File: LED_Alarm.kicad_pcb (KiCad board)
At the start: 2 copper layers, 48.3 x 82.8 mm, 83 parts, among them Q301 Q_NPN_BCE, Q401 FDMA410NZT, Q402 FDMA410NZT, Q403 FDMA410NZT, Q501 FDMA410NZT, Q502 FDMA410NZT, Q503 FDMA410NZT, Q601 FDMA410NZT, Q602 FDMA410NZT, Q603 FDMA410NZT, Q701 FDMA410NZT, Q702 FDMA410NZT, Q703 FDMA410NZT, Q801 FDMA410NZT, Q802 FDMA410NZT, Q803 FDMA410NZT, U101 H11AA11, U102 ESP-12, U103 PCA9685PW, U201 MOC3020M, U202 TRIAC, U901 XC9263

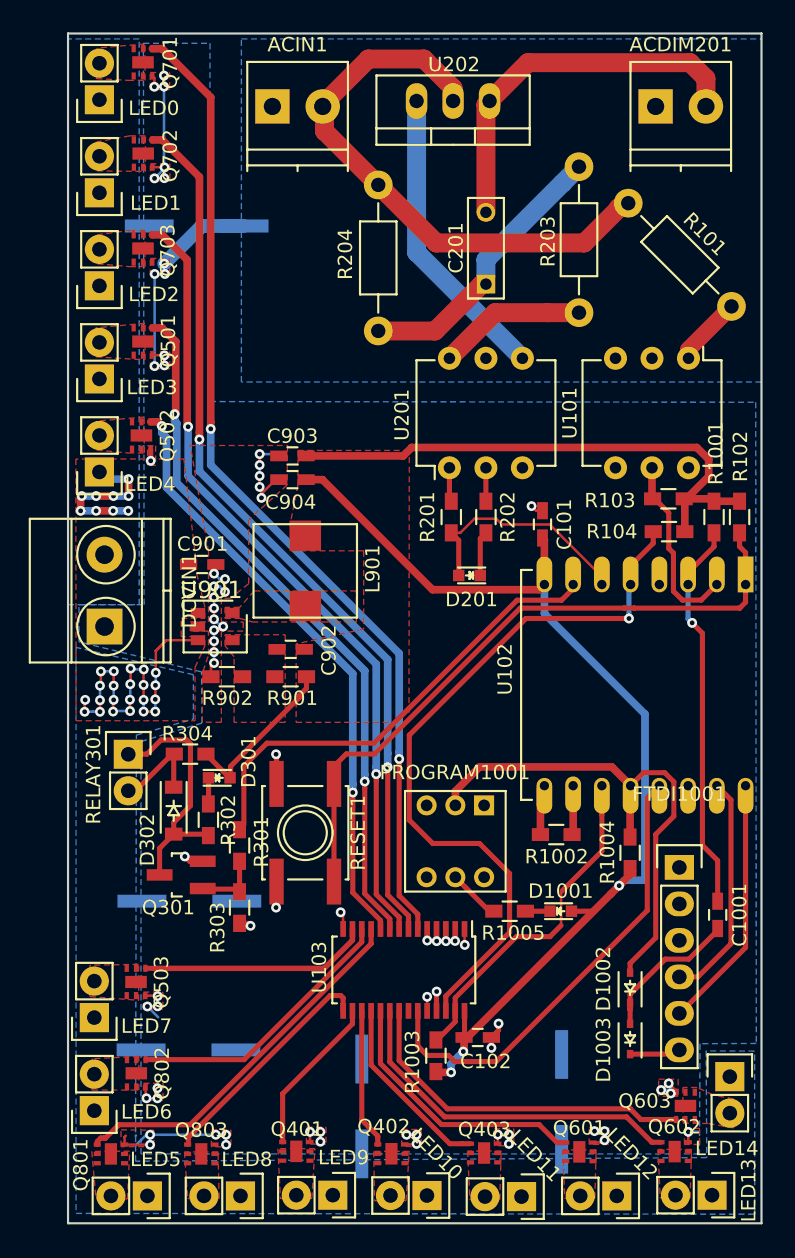
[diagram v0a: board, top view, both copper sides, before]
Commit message: After changes suggested in https://www.reddit.com/r/PrintedCircuitBoard/comments/54ctxv/pcb_review_of_a_pwm_esp8266_led_driver_board/
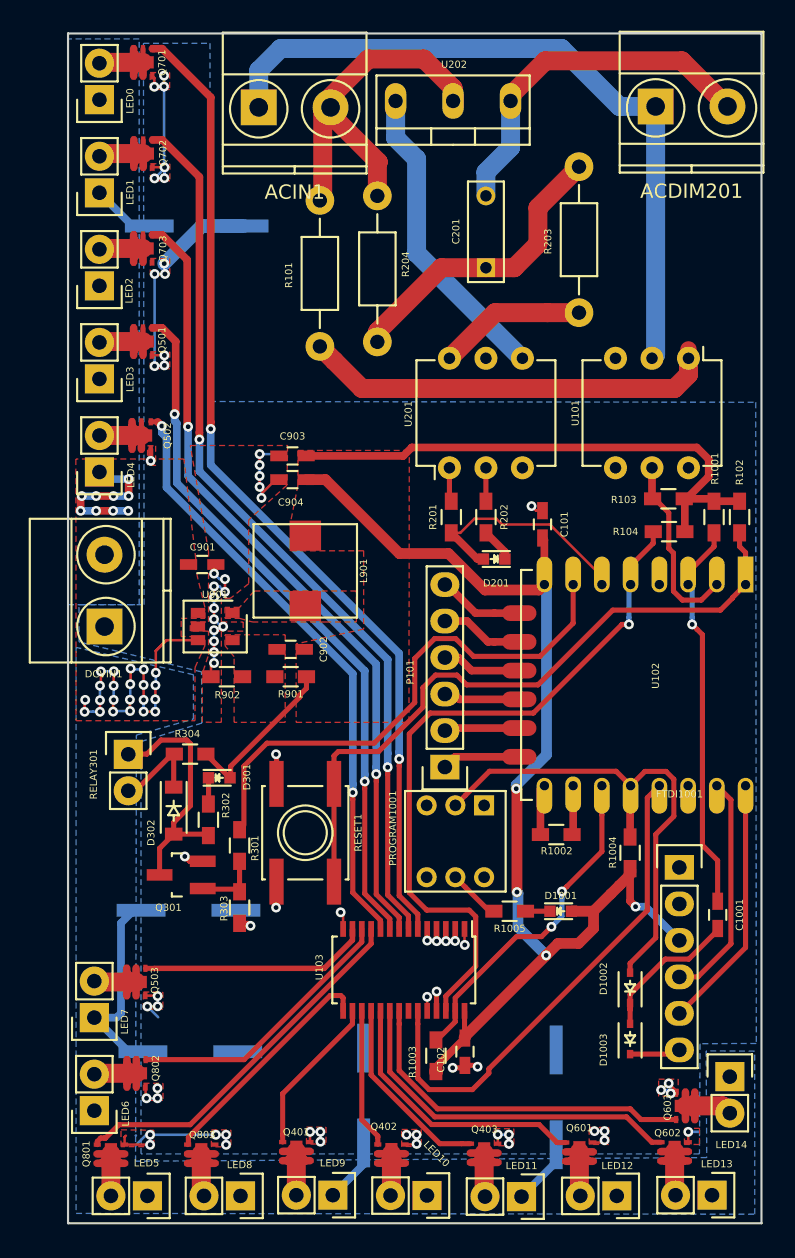
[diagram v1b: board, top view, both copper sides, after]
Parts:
- added P101: CONN_01X06, Pin_Headers:Pin_Header_Straight_1x06, F.Cu at (78.3, 88.8)
- ACDIM201, ACIN1: footprint Terminal_Blocks:TerminalBlock_Pheonix_PT-3.5mm_2pol -> Terminal_Blocks:TerminalBlock_Pheonix_MKDS1.5-2pol
- U102: footprint ESP8266:ESP-12 -> ESP8266:ESP-12E
- moved R101 21.5 mm to (69.6, 49.3), turned to 270 degrees
- moved D201 2.06 mm to (81.7, 74.3)
- moved C102 1.33 mm to (79.7, 108.6), turned to 270 degrees
- moved C201 1.14 mm to (81.2, 54.0)
- moved ACIN1 0.95 mm to (65.3, 42.9)
- moved C601 0.77 mm to (72.6, 111.6)
- moved R204 0.76 mm to (73.6, 59.2)
- moved C501 0.64 mm to (60.5, 98.7)
- moved C801 0.50 mm to (86.0, 111.8)
- moved C401 0.18 mm to (60.6, 108.6)
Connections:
- FTDI1001 pad 3: Net-(FTDI1001-Pad3) -> +3V3
- U102 pad 10: /gpio15 -> Net-(P101-Pad5)
- U102 pad 11: /I2C_SDA -> Net-(P101-Pad4)
- U102 pad 12: /gpio0 -> Net-(P101-Pad3)
- U102 pad 13: Net-(U102-Pad13) -> Net-(P101-Pad2)
- U102 pad 15: /rx -> GNDREF
- U102 pad 16: /tx -> /gpio15
- U102 pad 9: GNDREF -> Net-(P101-Pad6)
- U103 pad 23: Net-(U102-Pad13) -> Net-(U102-Pad19)
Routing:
- net GNDPWR: track 0.00 -> 50.1 mm
- net Net-(U102-Pad19): track 0.00 -> 35.4 mm
- net Net-(U102-Pad13): track 32.3 -> 0.00 mm
- net +12V: track 36.9 -> 64.8 mm
- net Net-(R101-Pad2): track 4.85 -> 29.0 mm
- net HT: track 38.7 -> 26.4 mm
- net Net-(LED14-Pad2): track 0.00 -> 7.64 mm
- net +3V3: track 124.7 -> 132.3 mm, vias 3 -> 4
- net Net-(LED1-Pad2): track 0.00 -> 7.46 mm
- net Net-(LED12-Pad2): track 0.00 -> 7.43 mm
- net Net-(LED0-Pad2): track 0.00 -> 7.40 mm
- net Net-(LED13-Pad2): track 0.00 -> 7.40 mm
- net Net-(LED2-Pad2): track 0.00 -> 7.40 mm
- net Net-(LED3-Pad2): track 0.00 -> 7.40 mm
- net Net-(LED11-Pad2): track 0.00 -> 7.40 mm
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- removed copper zone on B.Cu, net GNDPWR
- removed copper zone on F.Cu, net Net-(LED0-Pad2)
- removed copper zone on F.Cu, net Net-(LED1-Pad2)
- removed copper zone on F.Cu, net Net-(LED10-Pad2)
- removed copper zone on F.Cu, net Net-(LED11-Pad2)
- removed copper zone on F.Cu, net Net-(LED12-Pad2)
- removed copper zone on F.Cu, net Net-(LED13-Pad2)
- removed copper zone on F.Cu, net Net-(LED14-Pad2)
- removed copper zone on F.Cu, net Net-(LED2-Pad2)
- removed copper zone on F.Cu, net Net-(LED3-Pad2)
- removed copper zone on F.Cu, net Net-(LED4-Pad2)
- removed copper zone on F.Cu, net Net-(LED5-Pad2)
- removed copper zone on F.Cu, net Net-(LED6-Pad2)
- removed copper zone on F.Cu, net Net-(LED7-Pad2)
- removed copper zone on F.Cu, net Net-(LED8-Pad2)
- removed copper zone on F.Cu, net Net-(LED9-Pad2)
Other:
- net class GNDPWR: clearance 0.4 -> 1.3
- net class HT: clearance 0.4 -> 1.3
- rule pad_to_mask_clearance: 0.2 -> 0.1

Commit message: changed some stuff around
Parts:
- added F101: PRG18BB101MB1RB, Resistors_SMD:R_0603_HandSoldering, F.Cu at (71.3, 62.4)
- added VR101: MOV-07D221K-ND, Varistors:RV_Disc_D9_W3.5_P5, F.Cu at (75.6, 45.1)
- moved U202 5.59 mm to (84.5, 42.4)
- moved P101 0.51 mm to (78.3, 88.3)
- moved R204 0.25 mm to (73.6, 59.4)
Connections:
- R101 pad 2: Net-(R101-Pad2) -> Net-(F101-Pad2)
- U101 pad 1: Net-(R101-Pad2) -> Net-(F101-Pad1)
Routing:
- net Net-(R101-Pad2): track 29.0 -> 0.00 mm
- net Net-(F101-Pad1): track 0.00 -> 24.3 mm
- net Net-(F101-Pad2): track 0.00 -> 3.18 mm
- net GNDPWR: track 50.1 -> 52.1 mm
- net HT: track 26.4 -> 25.2 mm
- net Net-(C201-Pad1): track 21.0 -> 20.2 mm
- net /AC_CTRL2: track 36.6 -> 37.2 mm
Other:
- board size 48.3 x 82.8 mm -> 48.8 x 83.3 mm
- rule pad_to_mask_clearance: 0.1 -> 0.0762
